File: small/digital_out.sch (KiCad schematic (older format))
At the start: 9 parts, among them U11 EL357N(C)(TA)-G, U12 EL357N(C)(TA)-G, U13 ASSR-1218, U15 ASSR-1218, U18 ULN2003A

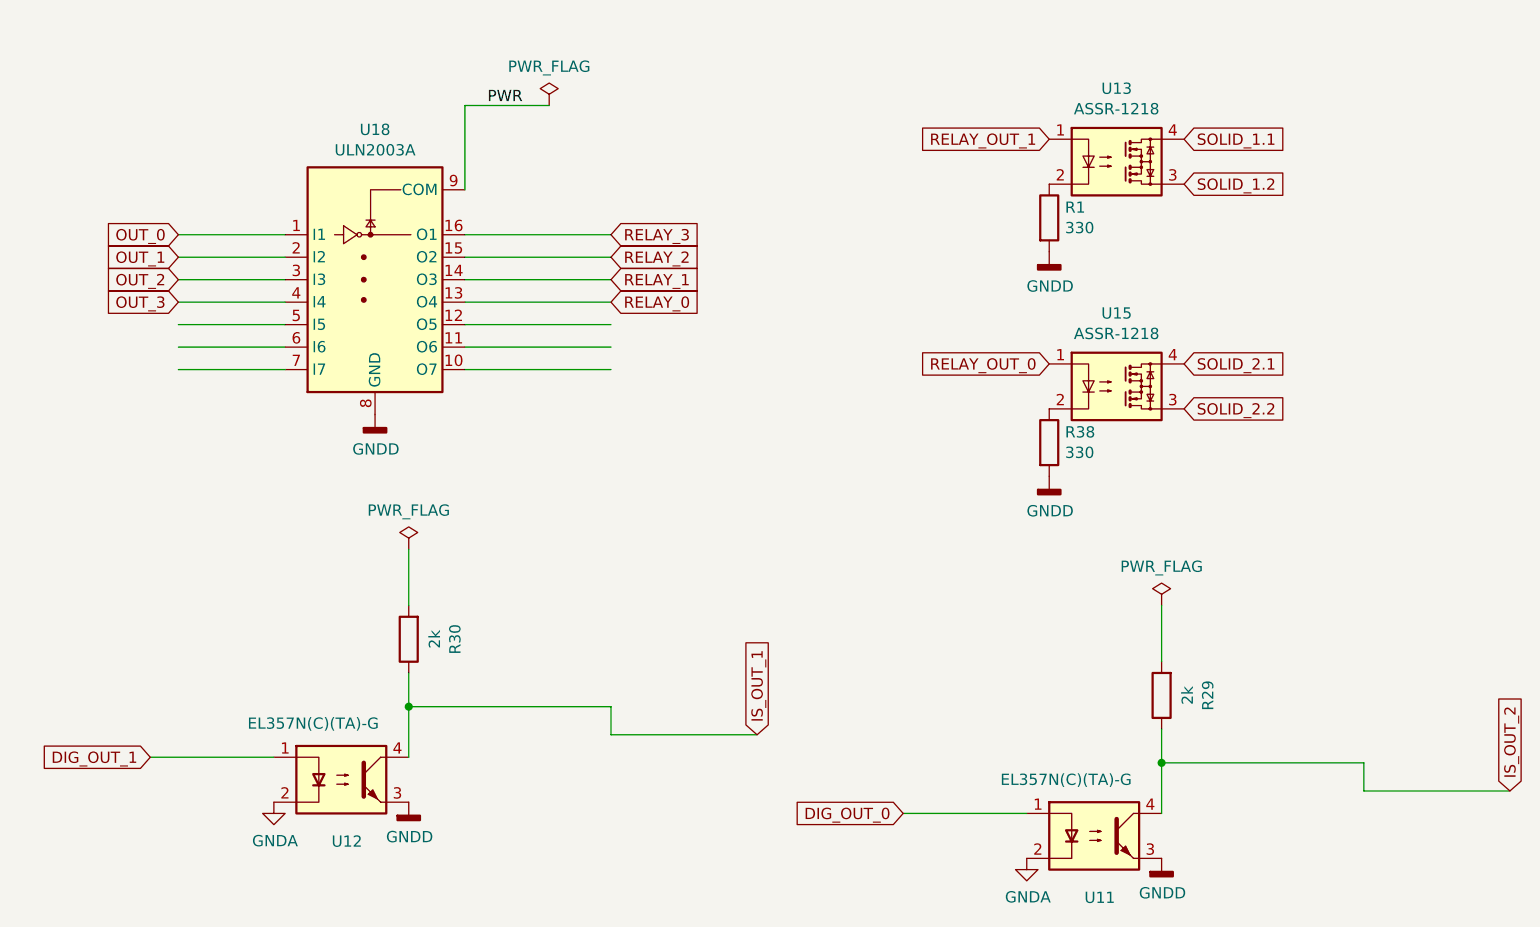
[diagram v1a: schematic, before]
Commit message: GPS connector moved,
antenna matching networks removed

SUPERCAPACITOR from jlpcb used.
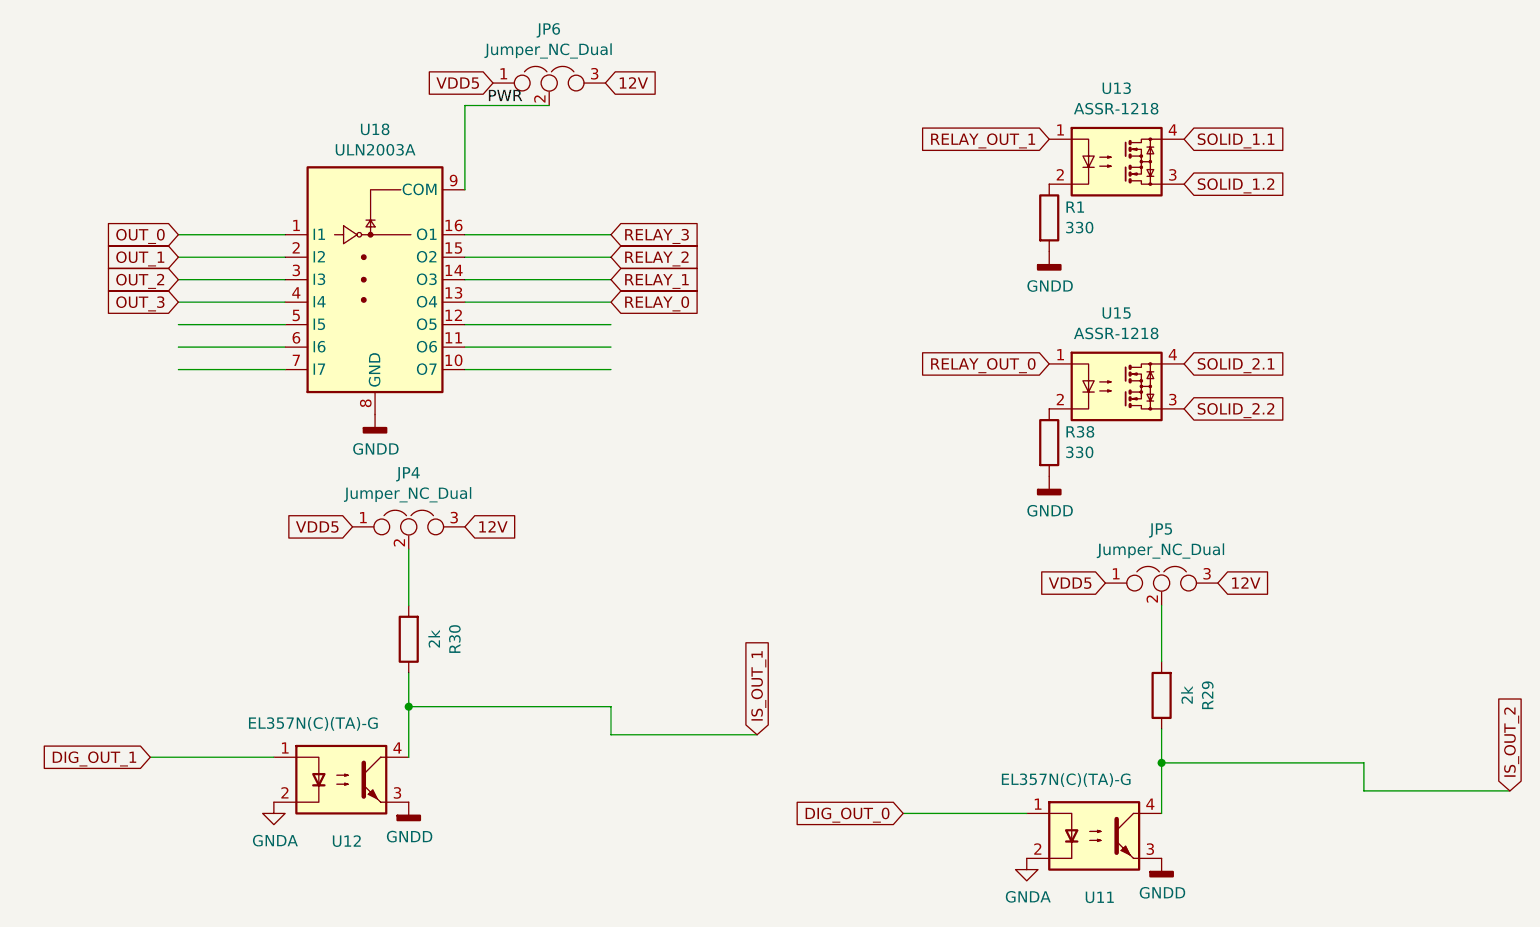
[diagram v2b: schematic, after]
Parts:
- added JP4, JP5, JP6: Jumper_NC_Dual, Jumper:SolderJumper-3_P1.3mm_Open_Pad1.0x1.5mm, symbol Device:Jumper_NC_Dual
- U11, U12: LCSC (none) -> C29981; LCSC# C29981 -> (none)
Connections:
- net labels added: 12V, VDD5
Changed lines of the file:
@@
 Wire Wire Line
 	2575 1175 2950 1175
-Text Label 2675 1175 0    50   ~ 0
-PWR
 Wire Wire Line
 	2575 1175 2575 1550
@@
 Wire Wire Line
 	2575 2350 3225 2350
-$Comp
-L power:PWR_FLAG #FLG02
-U 1 1 6580B77A
-P 2950 1175
-F 0 "#FLG02" H 2950 1250 50  0001 C CNN
-F 1 "PWR_FLAG" H 2950 1348 50  0000 C CNN
-F 2 "" H 2950 1175 50  0001 C CNN
-F 3 "~" H 2950 1175 50  0001 C CNN
-	1    2950 1175
-	1    0    0    -1
-$EndComp
 Text GLabel 1300 1750 0    50   Input ~ 0
 OUT_0
@@
 F 4 "$0.0520" H 2025 4175 50  0001 C CNN "CMPN"
 F 5 "EL357N(C)(TA)-G" H 2025 4175 50  0001 C CNN "MPN"
-F 6 "C29981" H 2025 4175 50  0001 C CNN "LCSC#"
+F 6 "" H 2025 4175 50  0001 C CNN "LCSC#"
+F 7 "C29981" H 2025 4175 50  0001 C CNN "LCSC"
 	1    2025 4175
 	1    0    0    -1
 $EndComp
-Wire Wire Line
-	2325 3150 2325 3400
 $Comp
 L Device:R R?
@@
 F 4 "$0.0520" H 5375 4425 50  0001 C CNN "CMPN"
 F 5 "EL357N(C)(TA)-G" H 5375 4425 50  0001 C CNN "MPN"
-F 6 "C29981" H 5375 4425 50  0001 C CNN "LCSC#"
+F 6 "" H 5375 4425 50  0001 C CNN "LCSC#"
+F 7 "C29981" H 5375 4425 50  0001 C CNN "LCSC"
 	1    5375 4425
 	1    0    0    -1
 $EndComp
-Wire Wire Line
-	5675 3400 5675 3650
 Connection ~ 5675 4100
 Wire Wire Line
@@
 Text GLabel 1175 4075 0    50   Input ~ 0
 DIG_OUT_1
-$Comp
-L power:PWR_FLAG #FLG0101
-U 1 1 609F8CB6
-P 2325 3150
-F 0 "#FLG0101" H 2325 3225 50  0001 C CNN
-F 1 "PWR_FLAG" H 2325 3323 50  0000 C CNN
-F 2 "" H 2325 3150 50  0001 C CNN
-F 3 "~" H 2325 3150 50  0001 C CNN
-	1    2325 3150
-	1    0    0    -1
-$EndComp
-$Comp
-L power:PWR_FLAG #FLG0102
-U 1 1 609F9818
-P 5675 3400
-F 0 "#FLG0102" H 5675 3475 50  0001 C CNN
-F 1 "PWR_FLAG" H 5675 3573 50  0000 C CNN
-F 2 "" H 5675 3400 50  0001 C CNN
-F 3 "~" H 5675 3400 50  0001 C CNN
-	1    5675 3400
-	1    0    0    -1
-$EndComp
 $Comp
 L Device:R R?
@@
 Text GLabel 5775 2525 2    50   Input ~ 0
 SOLID_2.2
+Wire Wire Line
+	5675 3400 5675 3650
+$Comp
+L Device:Jumper_NC_Dual JP5
+U 1 1 602FA9CA
+P 5675 3300
+F 0 "JP5" H 5675 3539 50  0000 C CNN
+F 1 "Jumper_NC_Dual" H 5675 3448 50  0000 C CNN
+F 2 "Jumper:SolderJumper-3_P1.3mm_Open_Pad1.0x1.5mm" H 5675 3300 50  0001 C CNN
+F 3 "~" H 5675 3300 50  0001 C CNN
+	1    5675 3300
+	1    0    0    -1
+$EndComp
+Text GLabel 5925 3300 2    50   Input ~ 0
+12V
+Text GLabel 5425 3300 0    50   Input ~ 0
+VDD5
+Text Label 2675 1175 0    50   ~ 0
+PWR
+Text GLabel 2075 3050 0    50   Input ~ 0
+VDD5
+Text GLabel 2575 3050 2    50   Input ~ 0
+12V
+$Comp
+L Device:Jumper_NC_Dual JP4
+U 1 1 602F1C4D
+P 2325 3050
+F 0 "JP4" H 2325 3289 50  0000 C CNN
+F 1 "Jumper_NC_Dual" H 2325 3198 50  0000 C CNN
+F 2 "Jumper:SolderJumper-3_P1.3mm_Open_Pad1.0x1.5mm" H 2325 3050 50  0001 C CNN
+F 3 "~" H 2325 3050 50  0001 C CNN
+	1    2325 3050
+	1    0    0    -1
+$EndComp
+Wire Wire Line
+	2325 3150 2325 3400
+Text GLabel 2700 1075 0    50   Input ~ 0
+VDD5
+Text GLabel 3200 1075 2    50   Input ~ 0
+12V
+$Comp
+L Device:Jumper_NC_Dual JP6
+U 1 1 60303017
+P 2950 1075
+F 0 "JP6" H 2950 1314 50  0000 C CNN
+F 1 "Jumper_NC_Dual" H 2950 1223 50  0000 C CNN
+F 2 "Jumper:SolderJumper-3_P1.3mm_Open_Pad1.0x1.5mm" H 2950 1075 50  0001 C CNN
+F 3 "~" H 2950 1075 50  0001 C CNN
+	1    2950 1075
+	1    0    0    -1
+$EndComp
 $EndSCHEMATC

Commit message: BOM updated
Layout changed
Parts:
- R1, R38, U11, U12: source (none) -> 0
- R29, R30: MPN (none) -> 0805W8F2001T5E; Price 0.0044 -> 0.0040; source (none) -> 0
- U13, U15: source (none) -> 1
- U18: MPN (none) -> ULN2003ADR; Mpn ULN2003ADR -> (none); Website mouser -> (none); source (none) -> 0
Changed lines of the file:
@@
 F 2 "Package_SO:SOIC-16W_5.3x10.2mm_P1.27mm" H 2225 1400 50  0001 L CNN
 F 3 "http://www.ti.com/lit/ds/symlink/uln2003a.pdf" H 2275 1750 50  0001 C CNN
-F 4 "ULN2003ADR" H 2175 1950 50  0001 C CNN "Mpn"
+F 4 "" H 2175 1950 50  0001 C CNN "Mpn"
 F 5 "0.1676" H 2175 1950 50  0001 C CNN "Price"
-F 6 "mouser" H 2175 1950 50  0001 C CNN "Website"
+F 6 "" H 2175 1950 50  0001 C CNN "Website"
 F 7 "C7512" H 2175 1950 50  0001 C CNN "LCSC"
+F 8 "ULN2003ADR" H 2175 1950 50  0001 C CNN "MPN"
+F 9 "0" H 2175 1950 50  0001 C CNN "source"
 	1    2175 1950
 	1    0    0    -1
@@
 F 5 "0.0019" H 5175 1675 50  0001 C CNN "Price"
 F 6 "0603WAF3300T5E" H 5175 1675 50  0001 C CNN "MPN"
+F 7 "0" H 5175 1675 50  0001 C CNN "source"
 	1    5175 1675
 	1    0    0    -1
@@
 F 6 "" H 2025 4175 50  0001 C CNN "LCSC#"
 F 7 "C29981" H 2025 4175 50  0001 C CNN "LCSC"
+F 8 "0" H 2025 4175 50  0001 C CNN "source"
 	1    2025 4175
 	1    0    0    -1
@@
 F 3 "https://datasheet.lcsc.com/szlcsc/Uniroyal-Elec-0805W8F2001T5E_C17604.pdf" H 2325 3550 50  0001 C CNN
 F 4 " C17604" V 2325 3550 50  0001 C CNN "LCSC"
-F 5 "0.0044" V 2325 3550 50  0001 C CNN "Price"
+F 5 "0.0040" V 2325 3550 50  0001 C CNN "Price"
+F 6 "0805W8F2001T5E" H 2325 3550 50  0001 C CNN "MPN"
+F 7 "0" H 2325 3550 50  0001 C CNN "source"
 	1    2325 3550
 	-1   0    0    1
@@
 F 6 "" H 5375 4425 50  0001 C CNN "LCSC#"
 F 7 "C29981" H 5375 4425 50  0001 C CNN "LCSC"
+F 8 "0" H 5375 4425 50  0001 C CNN "source"
 	1    5375 4425
 	1    0    0    -1
@@
 F 3 "https://datasheet.lcsc.com/szlcsc/Uniroyal-Elec-0805W8F2001T5E_C17604.pdf" H 5675 3800 50  0001 C CNN
 F 4 " C17604" V 5675 3800 50  0001 C CNN "LCSC"
-F 5 "0.0044" V 5675 3800 50  0001 C CNN "Price"
+F 5 "0.0040" V 5675 3800 50  0001 C CNN "Price"
+F 6 "0805W8F2001T5E" H 5675 3800 50  0001 C CNN "MPN"
+F 7 "0" H 5675 3800 50  0001 C CNN "source"
 	1    5675 3800
 	-1   0    0    1
@@
 F 5 "1.1349" H 5475 1425 50  0001 C CNN "Price"
 F 6 "AQY211EHAX" H 5475 1425 50  0001 C CNN "MPN"
+F 7 "1" H 5475 1425 50  0001 C CNN "source"
 	1    5475 1425
 	1    0    0    -1
@@
 F 5 "0.0019" H 5175 2675 50  0001 C CNN "Price"
 F 6 "0603WAF3300T5E" H 5175 2675 50  0001 C CNN "MPN"
+F 7 "0" H 5175 2675 50  0001 C CNN "source"
 	1    5175 2675
 	1    0    0    -1
@@
 F 5 "1.1349" H 5475 2425 50  0001 C CNN "Price"
 F 6 "AQY211EHAX" H 5475 2425 50  0001 C CNN "MPN"
+F 7 "1" H 5475 2425 50  0001 C CNN "source"
 	1    5475 2425
 	1    0    0    -1

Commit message: minor updates
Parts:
- U11, U12: Price (none) -> 0.0850
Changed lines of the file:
@@
 F 7 "C29981" H 2025 4175 50  0001 C CNN "LCSC"
 F 8 "0" H 2025 4175 50  0001 C CNN "source"
+F 9 "0.0850" H 2025 4175 50  0001 C CNN "Price"
 	1    2025 4175
 	1    0    0    -1
@@
 F 7 "C29981" H 5375 4425 50  0001 C CNN "LCSC"
 F 8 "0" H 5375 4425 50  0001 C CNN "source"
+F 9 "0.0850" H 5375 4425 50  0001 C CNN "Price"
 	1    5375 4425
 	1    0    0    -1

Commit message: ENC28j60 package changed to soic 28 17.9
TODO: route
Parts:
- JP4, JP5, JP6: LCSC (none) -> N/A
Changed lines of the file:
@@
 F 2 "Jumper:SolderJumper-3_P1.3mm_Open_Pad1.0x1.5mm" H 5675 3300 50  0001 C CNN
 F 3 "~" H 5675 3300 50  0001 C CNN
+F 4 "N/A" H 5675 3300 50  0001 C CNN "LCSC"
 	1    5675 3300
 	1    0    0    -1
@@
 F 2 "Jumper:SolderJumper-3_P1.3mm_Open_Pad1.0x1.5mm" H 2325 3050 50  0001 C CNN
 F 3 "~" H 2325 3050 50  0001 C CNN
+F 4 "N/A" H 2325 3050 50  0001 C CNN "LCSC"
 	1    2325 3050
 	1    0    0    -1
@@
 F 2 "Jumper:SolderJumper-3_P1.3mm_Open_Pad1.0x1.5mm" H 2950 1075 50  0001 C CNN
 F 3 "~" H 2950 1075 50  0001 C CNN
+F 4 "N/A" H 2950 1075 50  0001 C CNN "LCSC"
 	1    2950 1075
 	1    0    0    -1

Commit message: iso voltage update
minor changes
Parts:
- R29, R30: value 2k -> 1k; LCSC C17604 -> C17513; MPN 0805W8F2001T5E -> 0805W8F1001T5E
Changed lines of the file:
@@
 AR Path="/657E4F8F/609F3D7D" Ref="R30"  Part="1"
 F 0 "R30" V 2118 3550 50  0000 C CNN
-F 1 "2k" V 2209 3550 50  0000 C CNN
+F 1 "1k" V 2209 3550 50  0000 C CNN
 F 2 "Resistor_SMD:R_0805_2012Metric" V 2255 3550 50  0001 C CNN
-F 3 "https://datasheet.lcsc.com/szlcsc/Uniroyal-Elec-0805W8F2001T5E_C17604.pdf" H 2325 3550 50  0001 C CNN
-F 4 " C17604" V 2325 3550 50  0001 C CNN "LCSC"
+F 3 "https://datasheet.lcsc.com/szlcsc/Uniroyal-Elec-0805W8F1001T5E_C17513.pdf" H 2325 3550 50  0001 C CNN
+F 4 "C17513" V 2325 3550 50  0001 C CNN "LCSC"
 F 5 "0.0040" V 2325 3550 50  0001 C CNN "Price"
-F 6 "0805W8F2001T5E" H 2325 3550 50  0001 C CNN "MPN"
+F 6 "0805W8F1001T5E" H 2325 3550 50  0001 C CNN "MPN"
 F 7 "0" H 2325 3550 50  0001 C CNN "source"
 	1    2325 3550
@@
 AR Path="/657E4F8F/609FB495" Ref="R29"  Part="1"
 F 0 "R29" V 5468 3800 50  0000 C CNN
-F 1 "2k" V 5559 3800 50  0000 C CNN
+F 1 "1k" V 5559 3800 50  0000 C CNN
 F 2 "Resistor_SMD:R_0805_2012Metric" V 5605 3800 50  0001 C CNN
-F 3 "https://datasheet.lcsc.com/szlcsc/Uniroyal-Elec-0805W8F2001T5E_C17604.pdf" H 5675 3800 50  0001 C CNN
-F 4 " C17604" V 5675 3800 50  0001 C CNN "LCSC"
+F 3 "https://datasheet.lcsc.com/szlcsc/Uniroyal-Elec-0805W8F1001T5E_C17513.pdf" H 5675 3800 50  0001 C CNN
+F 4 "C17513" V 5675 3800 50  0001 C CNN "LCSC"
 F 5 "0.0040" V 5675 3800 50  0001 C CNN "Price"
-F 6 "0805W8F2001T5E" H 5675 3800 50  0001 C CNN "MPN"
+F 6 "0805W8F1001T5E" H 5675 3800 50  0001 C CNN "MPN"
 F 7 "0" H 5675 3800 50  0001 C CNN "source"
 	1    5675 3800

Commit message: ULN2003 footprint updated
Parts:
- U18: footprint Package_SO:SOIC-16W_5.3x10.2mm_P1.27mm -> Package_SO:SOIC-16_3.9x9.9mm_P1.27mm
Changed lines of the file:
@@
 F 0 "U18" H 2175 2617 50  0000 C CNN
 F 1 "ULN2003A" H 2175 2526 50  0000 C CNN
-F 2 "Package_SO:SOIC-16W_5.3x10.2mm_P1.27mm" H 2225 1400 50  0001 L CNN
+F 2 "Package_SO:SOIC-16_3.9x9.9mm_P1.27mm" H 2225 1400 50  0001 L CNN
 F 3 "http://www.ti.com/lit/ds/symlink/uln2003a.pdf" H 2275 1750 50  0001 C CNN
 F 4 "" H 2175 1950 50  0001 C CNN "Mpn"
